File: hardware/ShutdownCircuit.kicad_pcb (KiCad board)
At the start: 2 copper layers, 56.1 x 91 mm, 31 parts, among them J1 Conn_01x04_Pin, J2 Conn_01x04_Pin, J3 Conn_01x04_Pin, J4 Conn_01x04_Pin, J5 Conn_01x04_Pin, J6 Conn_01x04_Pin, K1 G5Q-1, K2 G5Q-1, Q1 BC547CTFR, U1 CD4093 Schmitt Trigger NAND, U2 CD4013_FlipFlop, U3 CD4081 AND

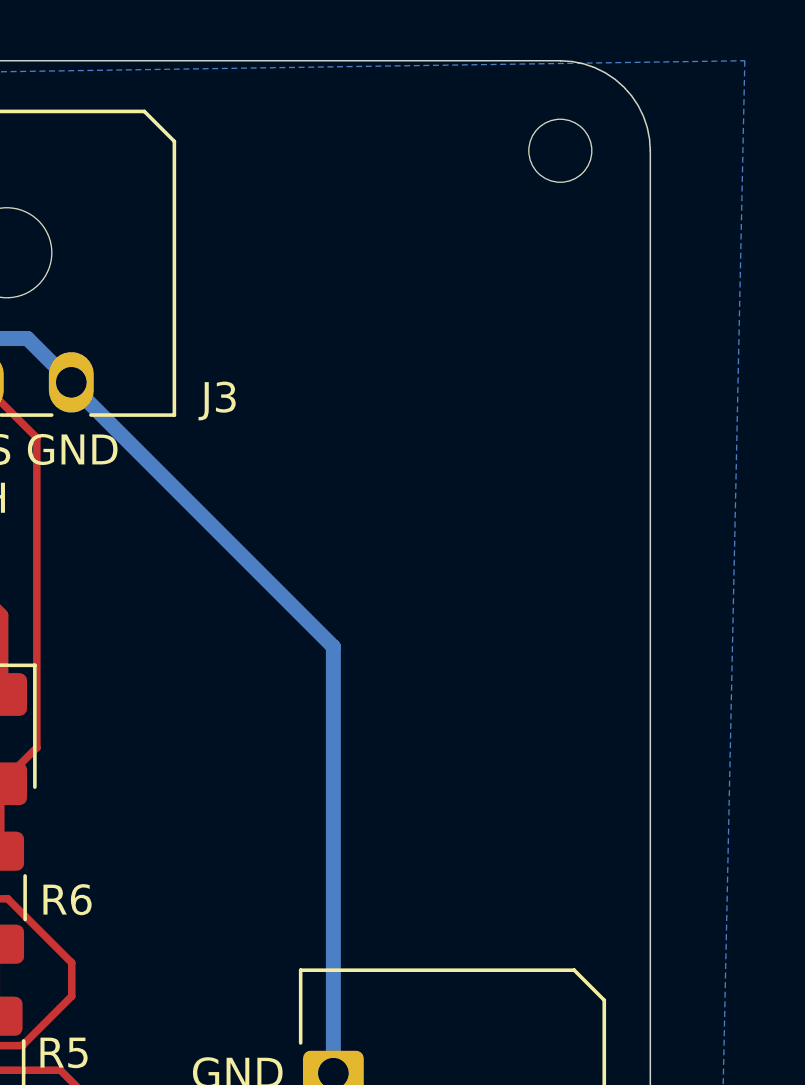
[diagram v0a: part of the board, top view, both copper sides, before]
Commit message: Added text on PCB
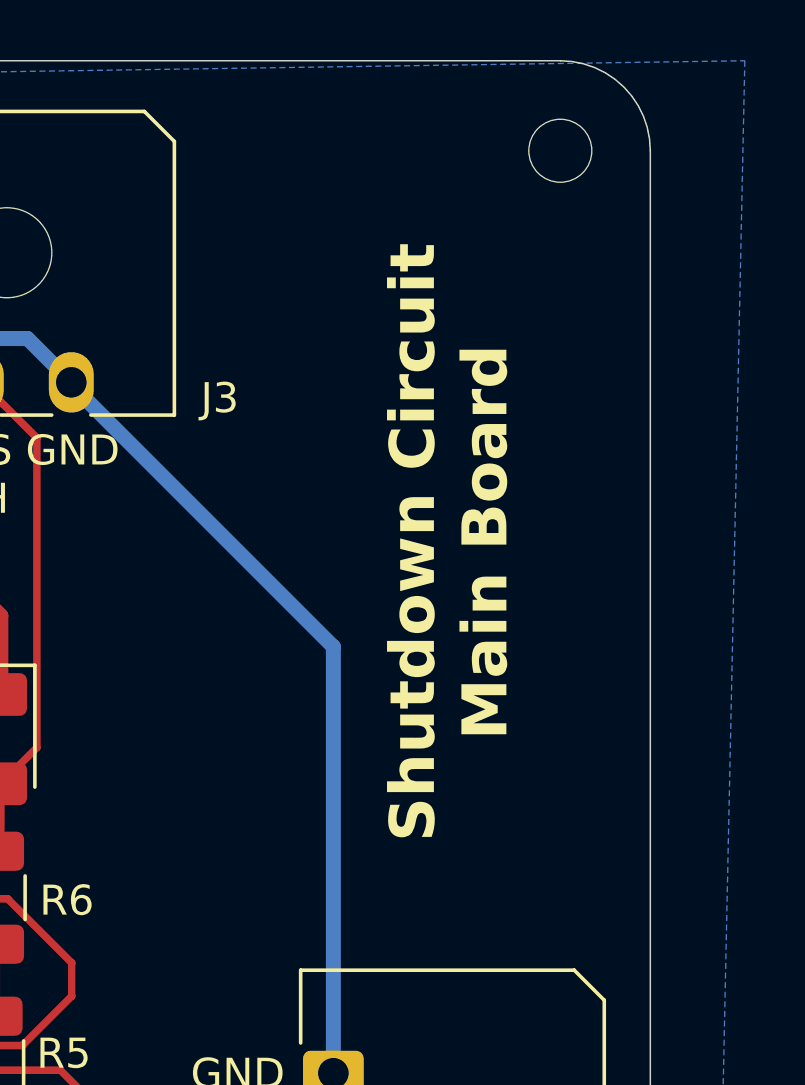
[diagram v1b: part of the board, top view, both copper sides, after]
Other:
- board text added: "Shutdown Circuit Main Board"
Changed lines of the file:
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@@
 	)
 	(paper "A4")
+	(title_block
+		(title "Shutdown Circuit Main Board")
+		(date "2026-05-06")
+		(company "Black Hornets Novi Sad - Ivan Berenic")
+	)
 	(layers
 		(0 "F.Cu" signal)
@@
 		)
 	)
+	(gr_text "Shutdown Circuit\nMain Board\n"
+		(at 137.65 84.65 90)
+		(layer "F.SilkS")
+		(effects
+			(font
+				(size 1.5 1.5)
+				(thickness 0.3)
+				(bold yes)
+			)
+		)
+	)

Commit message: Minor traces fixes
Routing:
- net +12V: track 163.1 -> 168.6 mm
- net GND: track 285.9 -> 287.6 mm
- net Net-(U1-H): track 9.54 -> 10.4 mm

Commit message: Traces fixed
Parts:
- C1: footprint Capacitor_SMD:C_1206_3216Metric -> Capacitor_SMD:C_1206_3216Metric_Pad1.33x1.80mm_HandSolder
- D1, D2: footprint Diode_SMD:D_SOD-523 -> Diode_SMD:D_1206_3216Metric_Pad1.42x1.75mm_HandSolder
- moved D1 0.99 mm to (122.2, 122.7)
- moved R8 0.90 mm to (111.8, 130.6)
- moved D5 0.66 mm to (111.7, 127.2)
- moved D3 0.60 mm to (109.3, 83.5)
- moved Q1 0.37 mm to (123.3, 118.0)
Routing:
- net GND: track 287.6 -> 316.1 mm, vias 8 -> 12
- net /AMS: track 54.4 -> 32.9 mm
- net Net-(U1-E): track 42.5 -> 22.8 mm
- net +12V: track 168.6 -> 180.1 mm
- net /IMD&BSPD&AMS: track 5.25 -> 15.6 mm
- net /IMD&BSPD: track 15.8 -> 11.9 mm
- net Net-(U1-F): track 4.41 -> 6.75 mm
- net /IMD: track 5.80 -> 6.70 mm
- net /IMD_DASHBOARD: track 12.3 -> 13.1 mm
- net /TSAL: track 23.7 -> 23.0 mm
- net Net-(J6-Pin_1): track 22.2 -> 22.8 mm
- net Net-(U1-G): track 5.48 -> 6.06 mm
- net /BSPD: track 16.6 -> 17.2 mm

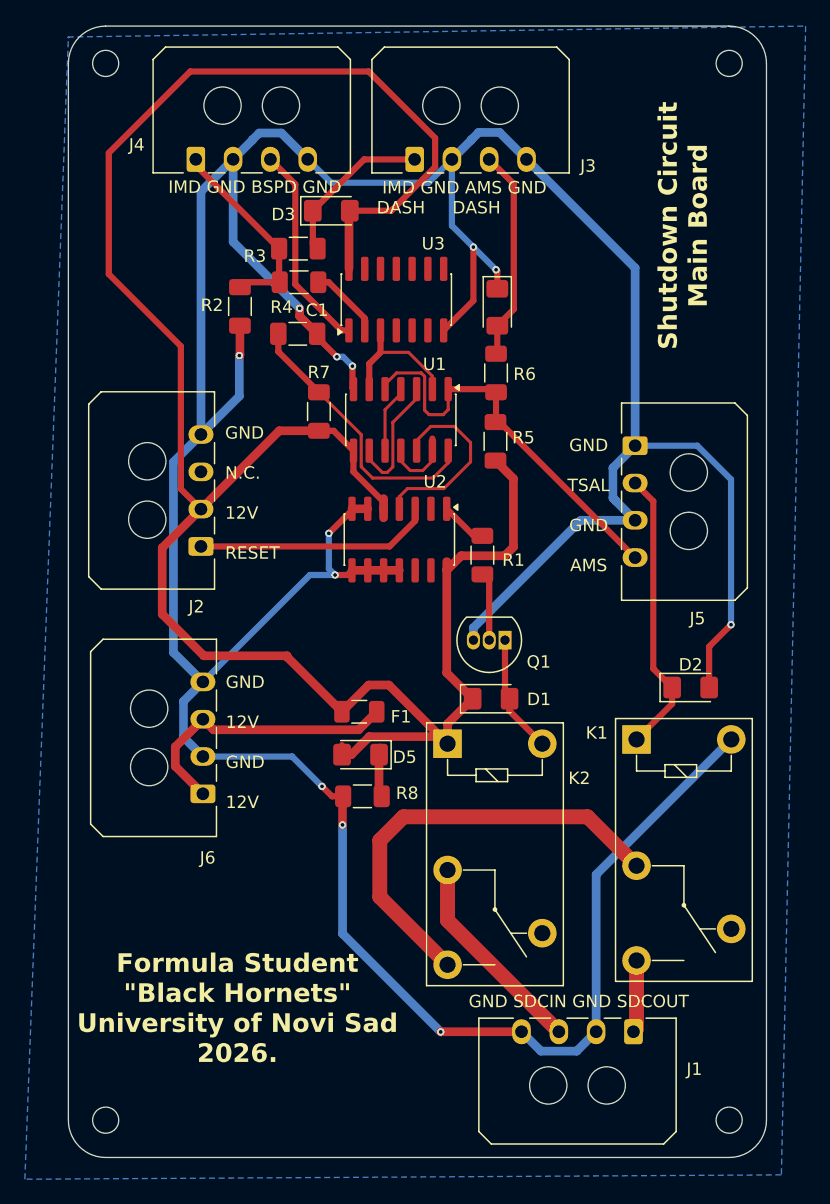
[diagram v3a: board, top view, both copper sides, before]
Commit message: Fill zone deleted. Duddy fix it please
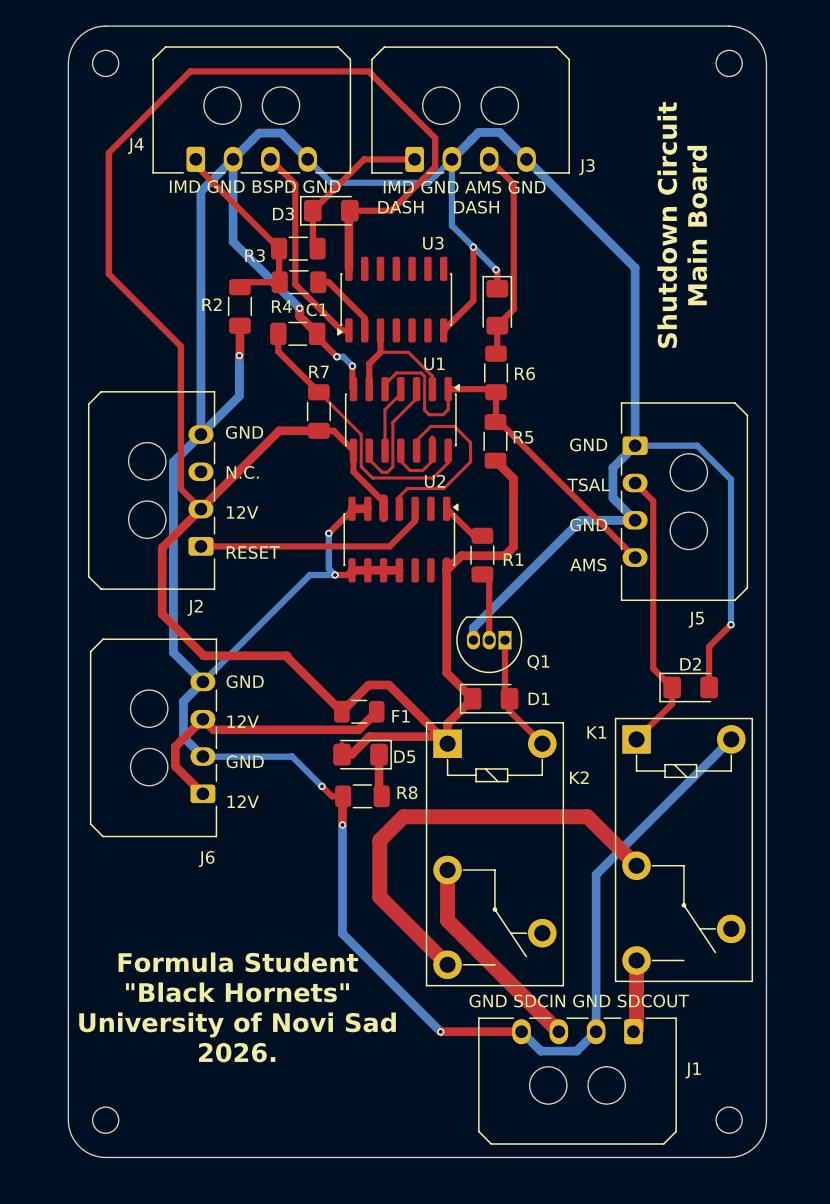
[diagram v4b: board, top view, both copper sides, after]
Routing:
- removed copper zone on B.Cu, net GND
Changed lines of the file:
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@@
 		(net 38)
-	)
-	(zone
-		(net 1)
-		(net_name "GND")
-		(layer "B.Cu")
-		(hatch edge 0.5)
-		(connect_pads
-			(clearance 0.3)
-		)
-		(min_thickness 0.25)
-		(filled_areas_thickness no)
-		(fill yes
-			(thermal_gap 0.5)
-			(thermal_bridge_width 0.5)
-		)
-		(polygon
-			(pts
-				(xy 88.15 69.47868) (xy 147.5 68.6) (xy 145.55 161) (xy 84.7 161.35) (xy 88.2 69.47868) (xy 88.25 69.55)
-			)
-		)
 	)
 	(embedded_fonts no)

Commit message: Added Back layer GND Fill zone for the board
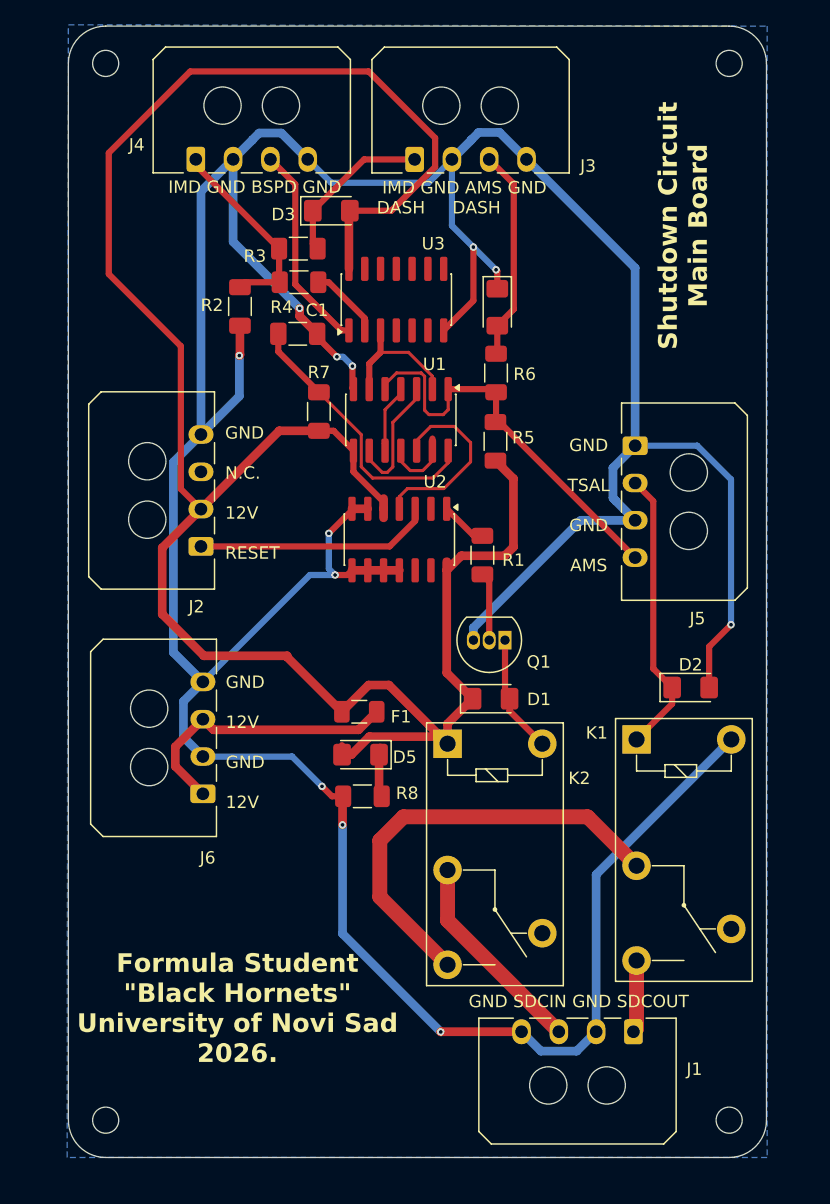
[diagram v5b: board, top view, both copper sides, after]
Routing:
- added copper zone on B.Cu, net GND
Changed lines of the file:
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@@
 		(net 38)
+	)
+	(zone
+		(net 1)
+		(net_name "GND")
+		(layer "B.Cu")
+		(hatch edge 0.5)
+		(connect_pads
+			(clearance 0.5)
+		)
+		(min_thickness 0.25)
+		(filled_areas_thickness no)
+		(fill yes
+			(thermal_gap 0.5)
+			(thermal_bridge_width 0.5)
+		)
+		(polygon
+			(pts
+				(xy 88.2 68.5) (xy 144.4 68.6) (xy 144.4 159.6) (xy 88.1 159.6)
+			)
+		)
 	)
 	(embedded_fonts no)

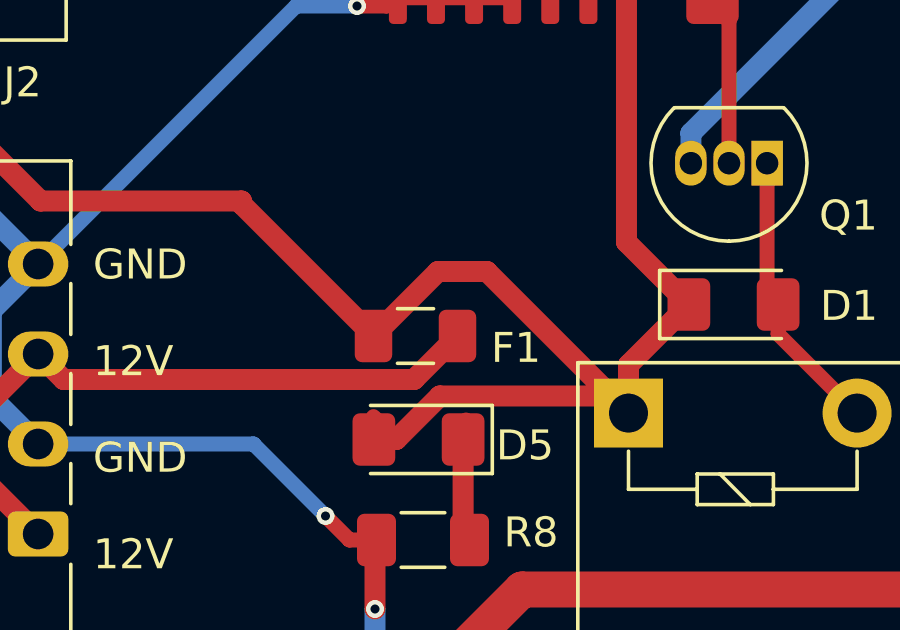
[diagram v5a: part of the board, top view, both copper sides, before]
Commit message: Fuse -> HandSoldered
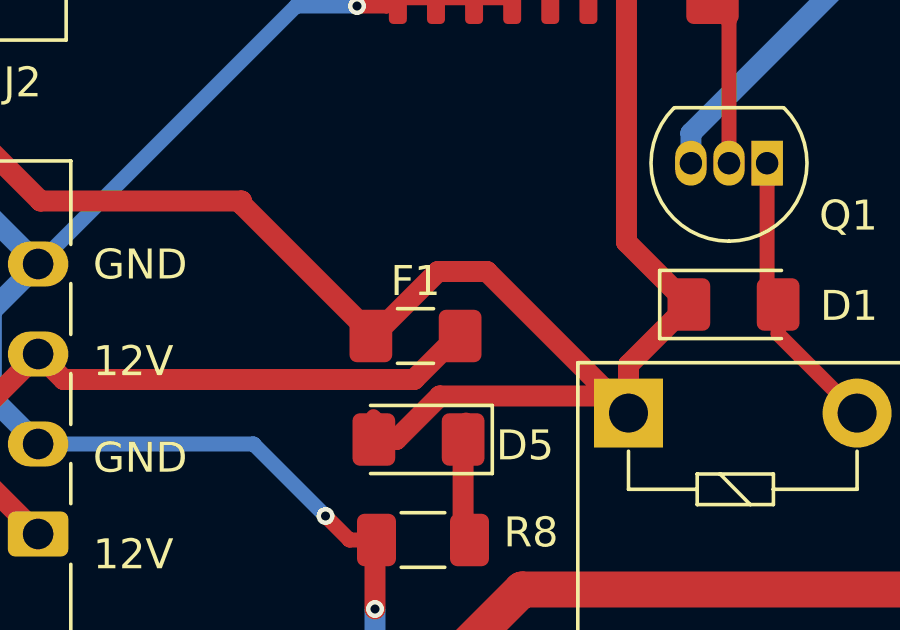
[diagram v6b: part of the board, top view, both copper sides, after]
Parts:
- F1: footprint Fuse:Fuse_1206_3216Metric -> Fuse:Fuse_1206_3216Metric_Pad1.42x1.75mm_HandSolder
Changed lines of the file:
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@@
 		)
 	)
-	(footprint "Fuse:Fuse_1206_3216Metric"
+	(footprint "Fuse:Fuse_1206_3216Metric_Pad1.42x1.75mm_HandSolder"
 		(layer "F.Cu")
 		(at 111.6 123.75)
-		(descr "Fuse SMD 1206 (3216 Metric), square (rectangular) end terminal, IPC-7351 nominal, (Body size source: http://www.tortai-tech.com/upload/download/2011102023233369053.pdf), generated with kicad-footprint-generator")
-		(tags "fuse")
+		(descr "Fuse SMD 1206 (3216 Metric), square (rectangular) end terminal, IPC-7351 nominal with elongated pad for handsoldering. (Body size source: http://www.tortai-tech.com/upload/download/2011102023233369053.pdf), generated with kicad-footprint-generator")
+		(tags "fuse handsolder")
 		(property "Reference" "F1"
-			(at 3.35 0.4 0)
+			(at 0 -1.83 0)
 			(layer "F.SilkS")
 			(effects
@@
 			(at 0 1.83 0)
 			(layer "F.Fab")
-			(hide yes)
 			(effects
 				(font
@@
 		)
 		(fp_rect
-			(start -2.28 -1.13)
-			(end 2.28 1.13)
+			(start -2.45 -1.13)
+			(end 2.45 1.13)
 			(stroke
 				(width 0.05)
@@
 		)
 		(pad "1" smd roundrect
-			(at -1.4 0)
-			(size 1.25 1.75)
+			(at -1.4875 0)
+			(size 1.425 1.75)
 			(layers "F.Cu" "F.Mask" "F.Paste")
-			(roundrect_rratio 0.2)
+			(roundrect_rratio 0.175439)
 			(net 3 "+12V")
 			(pintype "passive")
 		)
 		(pad "2" smd roundrect
-			(at 1.4 0)
-			(size 1.25 1.75)
+			(at 1.4875 0)
+			(size 1.425 1.75)
 			(layers "F.Cu" "F.Mask" "F.Paste")
-			(roundrect_rratio 0.2)
+			(roundrect_rratio 0.175439)
 			(net 9 "Net-(J6-Pin_1)")
 			(pintype "passive")
